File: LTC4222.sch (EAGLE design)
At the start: 24 parts

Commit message: Forgot to save the first time
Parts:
- added U$3, U$4: 74HC1G86GW-Q100H, Baja_Parts_Lib:74HC1G86GW-Q100H
- added U$5: SN74HC74QPWRQ1, Baja_Parts_Lib:SN74HC74QPWRQ1
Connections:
- new net N$1: U$3.A, U$3.Y, U$5.1D
- new net N$2: U$4.A, U$4.Y, U$5.2D
- new net N$3: U$12.EN2, U$5.2Q
- new net N$4: U$12.EN1, U$5.1Q
- net GND: now also U$3.GND, U$4.GND, U$5.GND
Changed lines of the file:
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@@
 <part name="U$1" library="Baja_Parts_Lib" deviceset="TNPW060310K0BEEN" device="" package3d_urn="urn:adsk.eagle:package:31668595/1"/>
 <part name="U$2" library="Baja_Parts_Lib" deviceset="TNPW060310K0BEEN" device="" package3d_urn="urn:adsk.eagle:package:31668595/1"/>
+<part name="U$3" library="Baja_Parts_Lib" deviceset="74HC1G86GW-Q100H" device="" package3d_urn="urn:adsk.eagle:package:31853395/1"/>
+<part name="U$4" library="Baja_Parts_Lib" deviceset="74HC1G86GW-Q100H" device="" package3d_urn="urn:adsk.eagle:package:31853395/1"/>
+<part name="U$5" library="Baja_Parts_Lib" deviceset="SN74HC74QPWRQ1" device="" package3d_urn="urn:adsk.eagle:package:31853367/1"/>
+<part name="SUPPLY6" library="supply2" library_urn="urn:adsk.eagle:library:372" deviceset="GND" device=""/>
+<part name="SUPPLY7" library="supply2" library_urn="urn:adsk.eagle:library:372" deviceset="GND" device=""/>
+<part name="SUPPLY8" library="supply2" library_urn="urn:adsk.eagle:library:372" deviceset="GND" device=""/>
 </parts>
 <sheets>
@@
 <attribute name="NAME" x="-254" y="-106.68" size="1.778" layer="95"/>
 <attribute name="VALUE" x="-254" y="-114.3" size="1.778" layer="96"/>
+</instance>
+<instance part="U$3" gate="G$1" x="-58.42" y="114.3" smashed="yes"/>
+<instance part="U$4" gate="G$1" x="-60.96" y="35.56" smashed="yes"/>
+<instance part="U$5" gate="G$1" x="-30.48" y="71.12" smashed="yes" rot="R270"/>
+<instance part="SUPPLY6" gate="GND" x="-68.58" y="17.78" smashed="yes">
+<attribute name="VALUE" x="-70.485" y="14.605" size="1.778" layer="96"/>
+</instance>
+<instance part="SUPPLY7" gate="GND" x="-66.04" y="96.52" smashed="yes">
+<attribute name="VALUE" x="-67.945" y="93.345" size="1.778" layer="96"/>
+</instance>
+<instance part="SUPPLY8" gate="GND" x="-53.34" y="73.66" smashed="yes">
+<attribute name="VALUE" x="-55.245" y="70.485" size="1.778" layer="96"/>
 </instance>
 </instances>
@@
 <wire x1="-165.1" y1="195.58" x2="-160.02" y2="195.58" width="0.1524" layer="91"/>
 <wire x1="-160.02" y1="195.58" x2="-160.02" y2="193.04" width="0.1524" layer="91"/>
+</segment>
+<segment>
+<pinref part="U$3" gate="G$1" pin="GND"/>
+<pinref part="SUPPLY7" gate="GND" pin="GND"/>
+<wire x1="-63.5" y1="101.6" x2="-66.04" y2="101.6" width="0.1524" layer="91"/>
+<wire x1="-66.04" y1="101.6" x2="-66.04" y2="99.06" width="0.1524" layer="91"/>
+</segment>
+<segment>
+<pinref part="U$4" gate="G$1" pin="GND"/>
+<wire x1="-66.04" y1="22.86" x2="-68.58" y2="22.86" width="0.1524" layer="91"/>
+<pinref part="SUPPLY6" gate="GND" pin="GND"/>
+<wire x1="-68.58" y1="22.86" x2="-68.58" y2="20.32" width="0.1524" layer="91"/>
+</segment>
+<segment>
+<pinref part="U$5" gate="G$1" pin="GND"/>
+<pinref part="SUPPLY8" gate="GND" pin="GND"/>
+<wire x1="-48.26" y1="76.2" x2="-53.34" y2="76.2" width="0.1524" layer="91"/>
 </segment>
 </net>
@@
 </segment>
 </net>
+<net name="N$1" class="0">
+<segment>
+<wire x1="-71.12" y1="91.44" x2="-71.12" y2="106.68" width="0.1524" layer="91"/>
+<pinref part="U$3" gate="G$1" pin="A"/>
+<wire x1="-71.12" y1="106.68" x2="-63.5" y2="106.68" width="0.1524" layer="91"/>
+<wire x1="-71.12" y1="91.44" x2="-35.56" y2="91.44" width="0.1524" layer="91"/>
+<wire x1="-35.56" y1="91.44" x2="-35.56" y2="76.2" width="0.1524" layer="91"/>
+<pinref part="U$5" gate="G$1" pin="1D"/>
+<pinref part="U$3" gate="G$1" pin="Y"/>
+<wire x1="-40.64" y1="101.6" x2="-35.56" y2="101.6" width="0.1524" layer="91"/>
+<wire x1="-35.56" y1="101.6" x2="-35.56" y2="91.44" width="0.1524" layer="91"/>
+</segment>
+</net>
+<net name="N$2" class="0">
+<segment>
+<pinref part="U$4" gate="G$1" pin="Y"/>
+<wire x1="-38.1" y1="22.86" x2="-43.18" y2="22.86" width="0.1524" layer="91"/>
+<wire x1="-38.1" y1="22.86" x2="-38.1" y2="12.7" width="0.1524" layer="91"/>
+<wire x1="-38.1" y1="12.7" x2="-73.66" y2="12.7" width="0.1524" layer="91"/>
+<wire x1="-73.66" y1="12.7" x2="-73.66" y2="27.94" width="0.1524" layer="91"/>
+<pinref part="U$4" gate="G$1" pin="A"/>
+<wire x1="-73.66" y1="27.94" x2="-66.04" y2="27.94" width="0.1524" layer="91"/>
+<pinref part="U$5" gate="G$1" pin="2D"/>
+<wire x1="-38.1" y1="48.26" x2="-38.1" y2="22.86" width="0.1524" layer="91"/>
+</segment>
+</net>
+<net name="N$3" class="0">
+<segment>
+<pinref part="U$5" gate="G$1" pin="2Q"/>
+<wire x1="-45.72" y1="48.26" x2="-45.72" y2="45.72" width="0.1524" layer="91"/>
+<pinref part="U$12" gate="G$1" pin="EN2"/>
+<wire x1="-45.72" y1="45.72" x2="-91.44" y2="45.72" width="0.1524" layer="91"/>
+</segment>
+</net>
+<net name="N$4" class="0">
+<segment>
+<pinref part="U$12" gate="G$1" pin="EN1"/>
+<wire x1="-91.44" y1="81.28" x2="-43.18" y2="81.28" width="0.1524" layer="91"/>
+<pinref part="U$5" gate="G$1" pin="1Q"/>
+<wire x1="-43.18" y1="81.28" x2="-43.18" y2="76.2" width="0.1524" layer="91"/>
+</segment>
+</net>

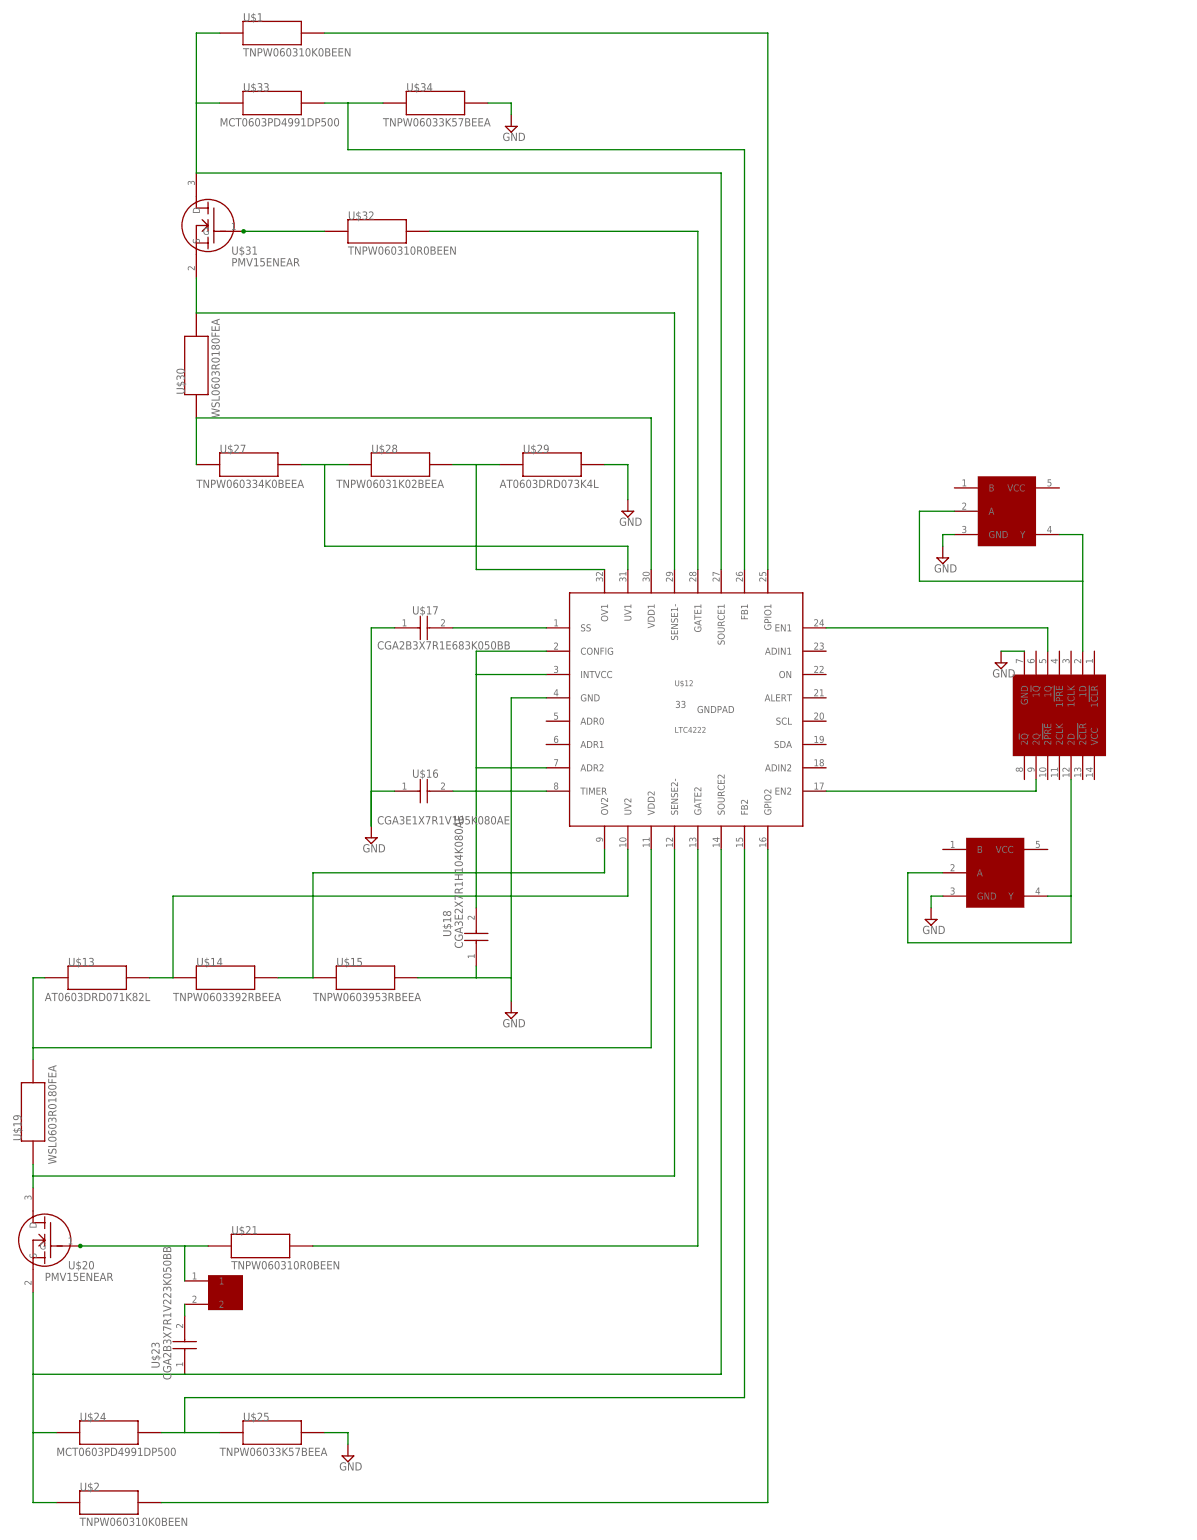
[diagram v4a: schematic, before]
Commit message: LTC4222 Schematic Design V2
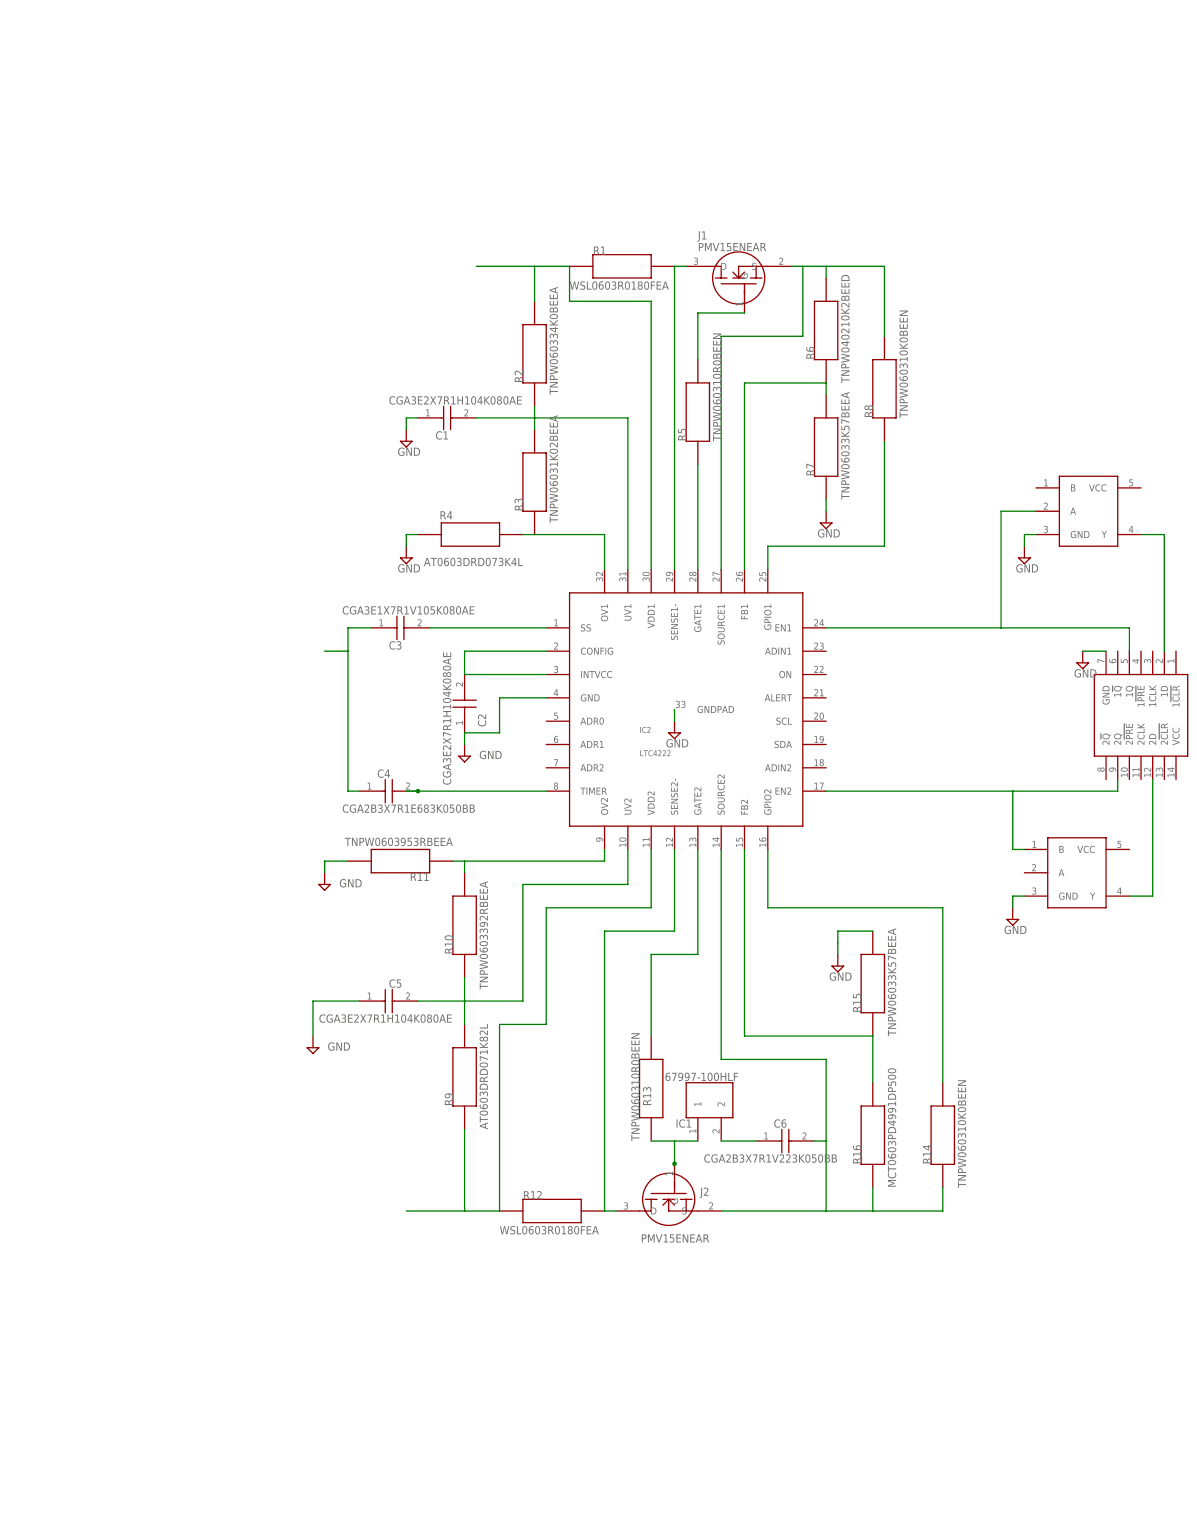
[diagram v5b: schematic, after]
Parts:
- removed U$1, U$2: TNPW060310K0BEEN, Baja_Parts_Lib:TNPW060310K0BEEN
- removed U$13: AT0603DRD071K82L, Baja_Parts_Lib:AT0603DRD071K82L
- removed U$14: TNPW0603392RBEEA, Baja_Parts_Lib:TNPW0603392RBEEA
- removed U$15: TNPW0603953RBEEA, Baja_Parts_Lib:TNPW0603953RBEEA
- removed U$16: CGA3E1X7R1V105K080AE, Baja_Parts_Lib:CGA3E1X7R1V105K080AE
- removed U$17: CGA2B3X7R1E683K050BB, Baja_Parts_Lib:CGA2B3X7R1E683K050BB
- removed U$18: CGA3E2X7R1H104K080AE, Baja_Parts_Lib:CGA3E2X7R1H104K080AE
- removed U$19, U$30: WSL0603R0180FEA, Baja_Parts_Lib:WSL0603R0180FEA
- removed U$20, U$31: PMV15ENEAR, Baja_Parts_Lib:PMV15ENEAR
- removed U$21, U$32: TNPW060310R0BEEN, Baja_Parts_Lib:TNPW060310R0BEEN
- removed U$22: 67997-100HLF, Baja_Parts_Lib:67997-100HLF
- removed U$23: CGA2B3X7R1V223K050BB, Baja_Parts_Lib:CGA2B3X7R1V223K050BB
- removed U$24, U$33: MCT0603PD4991DP500, Baja_Parts_Lib:MCT0603PD4991DP500
- removed U$25, U$34: TNPW06033K57BEEA, Baja_Parts_Lib:TNPW06033K57BEEA
- removed U$27: TNPW060334K0BEEA, Baja_Parts_Lib:TNPW060334K0BEEA
- removed U$28: TNPW06031K02BEEA, Baja_Parts_Lib:TNPW06031K02BEEA
- removed U$29: AT0603DRD073K4L, Baja_Parts_Lib:AT0603DRD073K4L
- added C1, C2, C5: CGA3E2X7R1H104K080AE, Baja_Parts_Lib:CGA3E2X7R1H104K080AE
- added C3: CGA3E1X7R1V105K080AE, Baja_Parts_Lib:CGA3E1X7R1V105K080AE
- added C4: CGA2B3X7R1E683K050BB, Baja_Parts_Lib:CGA2B3X7R1E683K050BB
- added C6: CGA2B3X7R1V223K050BB, Baja_Parts_Lib:CGA2B3X7R1V223K050BB
- added IC1: 67997-100HLF, Baja_Parts_Lib:67997-100HLF
- added J1, J2: PMV15ENEAR, Baja_Parts_Lib:PMV15ENEAR
- added R1, R12: WSL0603R0180FEA, Baja_Parts_Lib:WSL0603R0180FEA
- added R10: TNPW0603392RBEEA, Baja_Parts_Lib:TNPW0603392RBEEA
- added R11: TNPW0603953RBEEA, Baja_Parts_Lib:TNPW0603953RBEEA
- added R13, R5: TNPW060310R0BEEN, Baja_Parts_Lib:TNPW060310R0BEEN
- added R14, R8: TNPW060310K0BEEN, Baja_Parts_Lib:TNPW060310K0BEEN
- added R15, R7: TNPW06033K57BEEA, Baja_Parts_Lib:TNPW06033K57BEEA
- added R16: MCT0603PD4991DP500, Baja_Parts_Lib:MCT0603PD4991DP500
- added R2: TNPW060334K0BEEA, Baja_Parts_Lib:TNPW060334K0BEEA
- added R3: TNPW06031K02BEEA, Baja_Parts_Lib:TNPW06031K02BEEA
- added R4: AT0603DRD073K4L, Baja_Parts_Lib:AT0603DRD073K4L
- added R6: TNPW040210K2BEED, Baja_Parts_Lib:TNPW040210K2BEED
- added R9: AT0603DRD071K82L, Baja_Parts_Lib:AT0603DRD071K82L
- renumbered U$12 to IC2
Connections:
- removed net N$29: IC2.ADR2, IC2.CONFIG, IC2.INTVCC, U$18.2
- removed net N$30: IC2.VDD2, U$13.P$1, U$19.P$2
- removed net N$31: U$20.G, U$21.P$1, U$22.1
- removed net N$32: IC2.GATE2, U$21.P$2
- removed net N$33: U$22.2, U$23.2
- removed net N$34: IC2.SOURCE2, U$2.P$1, U$20.S, U$23.1, U$24.P$1
- removed net N$35: IC2.FB2, U$24.P$2, U$25.P$1
- removed net N$36: IC2.OV1, U$28.P$2, U$29.P$1
- removed net N$37: IC2.GPIO2, U$2.P$2
- removed net N$38: IC2.UV1, U$27.P$2, U$28.P$1
- removed net N$39: IC2.VDD1, U$27.P$1, U$30.P$1
- removed net N$40: IC2.SENSE1-, U$30.P$2, U$31.S
- removed net N$41: U$31.G, U$32.P$1
- removed net N$42: IC2.GATE1, U$32.P$2
- removed net N$43: IC2.SOURCE1, U$1.P$1, U$31.D, U$33.P$1
- removed net N$44: IC2.GPIO1, U$1.P$2
- removed net N$45: IC2.FB1, U$33.P$2, U$34.P$1
- new net N$10: C2.2, IC2.CONFIG, IC2.INTVCC
- new net N$11: IC2.GATE1, R5.P$1
- new net N$12: IC2.SOURCE1, J1.S, R6.P$2, R8.P$2
- new net N$13: IC2.FB1, R6.P$1, R7.P$2
- new net N$14: IC2.GPIO1, R8.P$1
- new net N$15: C4.2, IC2.TIMER
- new net N$16: C3.2, IC2.SS
- new net N$17: C3.1, C4.1
- new net N$18: IC2.GATE2, R13.P$2
- new net N$19: IC2.OV2, R10.P$2, R11.P$1
- new net N$20: IC2.SENSE2-, J2.D, R12.P$2
- new net N$21: IC2.VDD2, R12.P$1, R9.P$1
- new net N$22: IC1.1, J2.G, R13.P$1
- new net N$23: C6.2, IC2.SOURCE2, J2.S, R14.P$1, R16.P$1
- new net N$5: U$4.Y, U$5.2D
- new net N$6: IC2.SENSE1-, J1.D, R1.P$2
- new net N$7: IC2.OV1, R3.P$1, R4.P$1
- new net N$8: C1.2, IC2.UV1, R2.P$1, R3.P$2
- new net N$9: R5.P$2
- net GND: now also C1.1, C2.1, C5.1, R11.P$2, R4.P$2, R7.P$1; no longer U$15.P$2, U$16.1, U$17.1, U$18.1, U$25.P$2, U$29.P$2, U$34.P$2
- net N$1: no longer U$3.A
- net N$2: now also IC2.VDD1, R1.P$1, R2.P$2; no longer U$4.A, U$4.Y, U$5.2D
- net N$24: now also C6.1, IC1.2; no longer IC2.UV2, U$13.P$2, U$14.P$1
- net N$25: now also IC2.FB2, R15.P$1, R16.P$2; no longer IC2.OV2, U$14.P$2, U$15.P$1
- net N$26: now also IC2.GPIO2, R14.P$2; no longer IC2.TIMER, U$16.2
- net N$27: now also C5.2, IC2.UV2, R10.P$1, R9.P$2; no longer IC2.SS, U$17.2
- net N$28: now also R15.P$2; no longer IC2.SENSE2-, U$19.P$1, U$20.D
- net N$3: now also U$4.B
- net N$4: now also U$3.A
